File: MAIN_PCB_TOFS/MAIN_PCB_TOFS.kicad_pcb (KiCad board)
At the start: 2 copper layers, 60 x 84 mm, 13 parts, among them J1 Capteur Matricielle, J11 Capteur Matricielle, J12 SERVO m3, J13 SERVO m4, J2 Capteur Matricielle, J3 SERVO m2, J4 SERVO m1, J5 COMM_inter_mcu, U1 ESP32

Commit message: petites modifs kicad
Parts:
- added C1: 100n, Capacitor_SMD:C_0603_1608Metric, F.Cu at (126.2, 121.0)
- added C13: 100n, Capacitor_SMD:C_0603_1608Metric, F.Cu at (130.2, 121.0)
- added C2: 100u, Capacitor_SMD:CP_Elec_6.3x5.8, F.Cu at (109.1, 106.5)
- added C3: 100u, Capacitor_SMD:CP_Elec_6.3x5.8, F.Cu at (109.1, 114.6)
- added C4: 100u, Capacitor_SMD:CP_Elec_6.3x5.8, F.Cu at (109.1, 122.8)
- added C5: 10u, Capacitor_SMD:C_0603_1608Metric, F.Cu at (126.2, 123.5)
- added C6: 100n, Capacitor_SMD:C_0603_1608Metric, F.Cu at (126.2, 126.0)
- added C7: 100n, Capacitor_SMD:C_0603_1608Metric, F.Cu at (126.2, 128.5)
- added C8: 100n, Capacitor_SMD:C_0603_1608Metric, F.Cu at (126.2, 131.0)
- added D2: WS2812B, LED_SMD:LED_WS2812B_PLCC4_5.0x5.0mm_P3.2mm, F.Cu at (107.9, 130.2)
- added J1: TOF 2, Connector_PinHeader_2.54mm:PinHeader_1x06_P2.54mm_Vertical, F.Cu at (126.5, 104.7)
- added J2: TOF 3, Connector_PinHeader_2.54mm:PinHeader_1x06_P2.54mm_Vertical, F.Cu at (131.0, 104.7)
- added J6: TOF 1, Connector_PinHeader_2.54mm:PinHeader_1x06_P2.54mm_Vertical, F.Cu at (135.6, 104.7)
- added J7: Conn_01x02, Connector_PinHeader_2.54mm:PinHeader_1x02_P2.54mm_Vertical, F.Cu at (116.6, 125.4)
- added R1: 2.2k, Resistor_SMD:R_0603_1608Metric, F.Cu at (130.2, 123.5)
- added R2: 2.2k, Resistor_SMD:R_0603_1608Metric, F.Cu at (130.2, 126.0)
- added R3: 470R, Resistor_SMD:R_0603_1608Metric, F.Cu at (130.2, 128.5)
- added R4: 10k, Resistor_SMD:R_0603_1608Metric, F.Cu at (130.2, 131.0)
- added R5: 10k, Resistor_SMD:R_0603_1608Metric, F.Cu at (134.2, 121.0)
- added R6: 10k, Resistor_SMD:R_0603_1608Metric, F.Cu at (134.2, 123.5)
- added R7: 10k, Resistor_SMD:R_0603_1608Metric, F.Cu at (134.2, 126.0)
- added SW1: SW_SPDT, Button_Switch_SMD:SW_SPDT_PCM12, F.Cu at (119.2, 105.4)
- added SW2: SW_SPDT, Button_Switch_SMD:SW_SPDT_PCM12, F.Cu at (119.2, 112.3)
- added SW3: SW_SPDT, Button_Switch_SMD:SW_SPDT_PCM12, F.Cu at (119.2, 119.2)
- moved U1 12.6 mm to (97.6, 62.5)
- moved J1 8.94 mm to (133.0, 65.4)
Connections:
- U1 pad 11: unconnected-(U1-D35-Pad11) -> /Switch_terrain
- U1 pad 12: unconnected-(U1-D34-Pad12) -> /Switch_mode
- U1 pad 13: unconnected-(U1-UN-Pad13) -> /Tirette
- U1 pad 14: unconnected-(U1-UP-Pad14) -> /Switch_debug
- U1 pad 18: /SERVO_4 -> /SERVO_2
- U1 pad 19: /SERVO_3 -> unconnected-(U1-D2-Pad19)
- U1 pad 20: unconnected-(U1-D4-Pad20) -> /LPN2
- U1 pad 24: /SERVO_2 -> /LPN3
- U1 pad 30: unconnected-(U1-D23-Pad30) -> /LPN1
- U1 pad 5: /LED_IHM_2 -> /LED_IHM
- U1 pad 6: /LED_IHM_1 -> /SERVO_3
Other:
- board size 60 x 84 mm -> 88 x 84 mm

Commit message: organisation du pcb IHM pour préparer le routage
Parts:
- removed D4: GREEN_LED, LED_SMD:LED_0603_1608Metric
- removed D5: RED_LED, LED_SMD:LED_0603_1608Metric
- removed the J1 at (133.0, 65.4)
- removed J11: Capteur Matricielle, Connector_PinHeader_2.54mm:PinHeader_1x07_P2.54mm_Vertical
- removed J13: SERVO m4, Connector_PinHeader_2.54mm:PinHeader_1x03_P2.54mm_Vertical
- removed the J2 at (148.8, 65.1)
- removed R12, R13: 330R, Resistor_SMD:R_0603_1608Metric
- added H1: MountingHole_Pad, MountingHole:MountingHole_3.2mm_M3_Pad_Via, F.Cu at (83.5, 57.5)
- added H2: MountingHole_Pad, MountingHole:MountingHole_3.2mm_M3_Pad_Via, F.Cu at (139.4, 57.5)
- added H3: MountingHole_Pad, MountingHole:MountingHole_3.2mm_M3_Pad_Via, F.Cu at (139.4, 132.5)
- added H4: MountingHole_Pad, MountingHole:MountingHole_3.2mm_M3_Pad_Via, F.Cu at (83.5, 132.5)
- SW1: value SW_SPDT -> DEBUG
- SW2: value SW_SPDT -> TERRAIN
- SW3: value SW_SPDT -> MODE
- U1: footprint Library:PinHeader_2x15_P2.54mm_Vertical_esp32 -> Library:DIP-30_W25.4mm_LongPads_esp32
- moved J12 66.8 mm to (92.5, 57.7), turned to 90 degrees
- moved R7 66.0 mm to (86.0, 80.9), turned to 90 degrees
- moved J7 60.7 mm to (86.0, 73.0)
- moved C4 58.5 mm to (108.5, 64.3)
- moved C7 57.5 mm to (124.9, 71.0), turned to 180 degrees
- moved C3 52.3 mm to (95.0, 64.3)
- moved J3 47.2 mm to (105.7, 57.7), turned to 90 degrees
- moved R3 44.5 mm to (88.4, 113.1), turned to -90 degrees
- moved R1 44.1 mm to (125.7, 79.6), turned to -90 degrees
- moved C2 44.0 mm to (121.4, 64.3)
- moved C1 44.0 mm to (82.8, 113.7)
- moved C8 42.7 mm to (135.7, 89.4), turned to -90 degrees
- moved J4 40.9 mm to (118.3, 57.8), turned to 90 degrees
- moved R2 39.0 mm to (125.6, 87.2), turned to 90 degrees
- moved SW1 36.1 mm to (96.6, 133.5)
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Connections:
- J12 pad 1: /D18 -> /SERVO_3
- J3 pad 1: /D18 -> /SERVO_2
- J4 pad 1: /D19 -> /SERVO_1
- U1 pad 20: /LPN2 -> /LPN1
- U1 pad 30: /LPN1 -> /LPN2
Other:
- board size 88 x 84 mm -> 64.9 x 84 mm
- board text added: "Auto"
- board text added: "Bleu"
- board text added: "Jaune"
- board text added: "Manuel"
- board text added: "OFF"
- board text added: "ON"

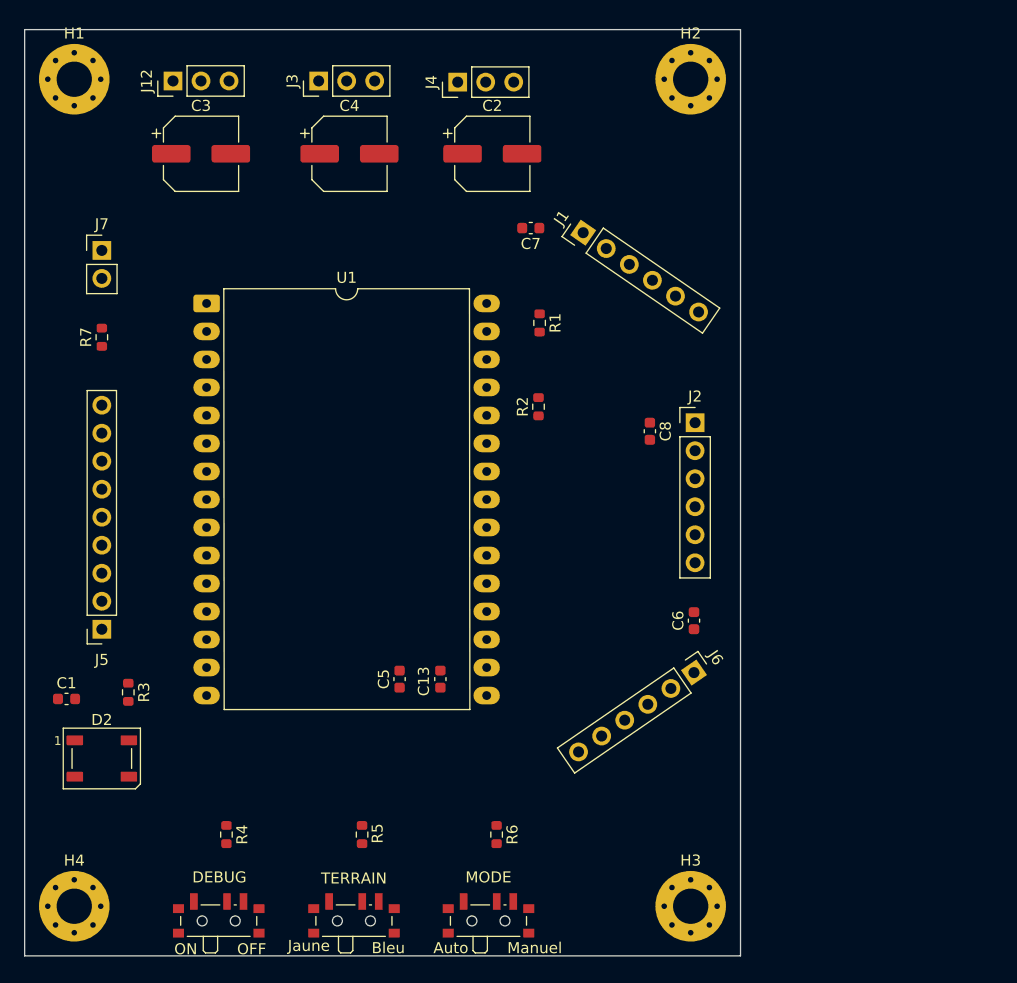
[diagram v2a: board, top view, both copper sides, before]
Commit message: modifications finales du pcb, problème sens capteurs tofs à régler
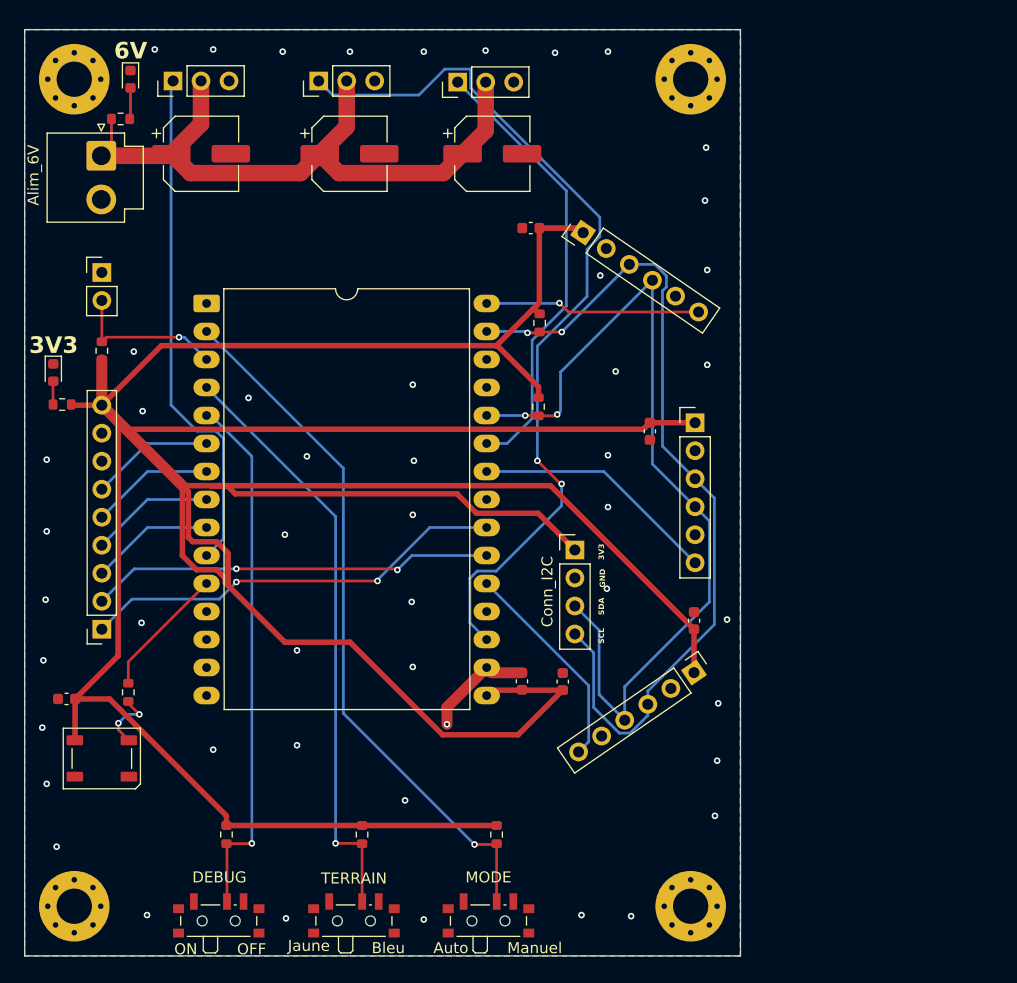
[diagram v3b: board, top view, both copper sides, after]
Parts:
- added D4: GREEN_LED, LED_SMD:LED_0603_1608Metric, F.Cu at (88.6, 57.5)
- added D5: GREEN_LED, LED_SMD:LED_0603_1608Metric, F.Cu at (81.6, 84.1)
- added J8: Alim_6V, Connector_JST:JST_VH_B2P-VH_1x02_P3.96mm_Vertical, F.Cu at (86.0, 64.4)
- added J9: Conn_I2C, Connector_PinHeader_2.54mm:PinHeader_1x04_P2.54mm_Vertical, F.Cu at (128.9, 100.2)
- added R12: 1k, Resistor_SMD:R_0603_1608Metric, F.Cu at (87.7, 61.1)
- added R13: 330R, Resistor_SMD:R_0603_1608Metric, F.Cu at (82.4, 87.0)
- moved C13 11.1 mm to (127.8, 112.1)
- moved C5 11.1 mm to (124.1, 112.1)
- moved J7 2.00 mm to (86.0, 75.0)
- moved R7 1.22 mm to (86.0, 82.1)
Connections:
- J5 pad 8: /6V -> unconnected-(J5-Pin_8-Pad8)
- U1 pad 11: /Switch_terrain -> /Switch_debug
- U1 pad 12: /Switch_mode -> /Switch_terrain
- U1 pad 14: /Switch_debug -> /Switch_mode
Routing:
- net /3V3: track 0.00 -> 369.6 mm
- net /SERVO_2: track 0.00 -> 80.3 mm, vias 0 -> 2
- net /SDA: track 0.00 -> 79.7 mm, vias 0 -> 2
- net /SCL: track 0.00 -> 77.7 mm, vias 0 -> 2
- net /Switch_mode: track 0.00 -> 63.9 mm, vias 0 -> 1
- net /6V: track 0.00 -> 62.2 mm
- net /Switch_terrain: track 0.00 -> 53.9 mm, vias 0 -> 1
- net /Switch_debug: track 0.00 -> 48.3 mm, vias 0 -> 1
- net /SERVO_3: track 0.00 -> 46.7 mm
- net /SERVO_1: track 0.00 -> 40.9 mm
- net /TX_ESP32: track 0.00 -> 38.8 mm, vias 0 -> 2
- net /RX_ESP32: track 0.00 -> 36.8 mm, vias 0 -> 2
- net /LPN3: track 0.00 -> 22.3 mm
- net /LPN2: track 0.00 -> 19.6 mm, vias 0 -> 1
- net /LPN1: track 0.00 -> 19.5 mm
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- added copper zone on B.Cu, net GND
- added copper zone on F.Cu, net GND
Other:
- board text added: "3V3"
- board text added: "6V"
- board text added: "GND"
- board text added: "SCL"
- board text added: "SDA"

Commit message: finalisation du pcb et création des fichiers nécéssaires
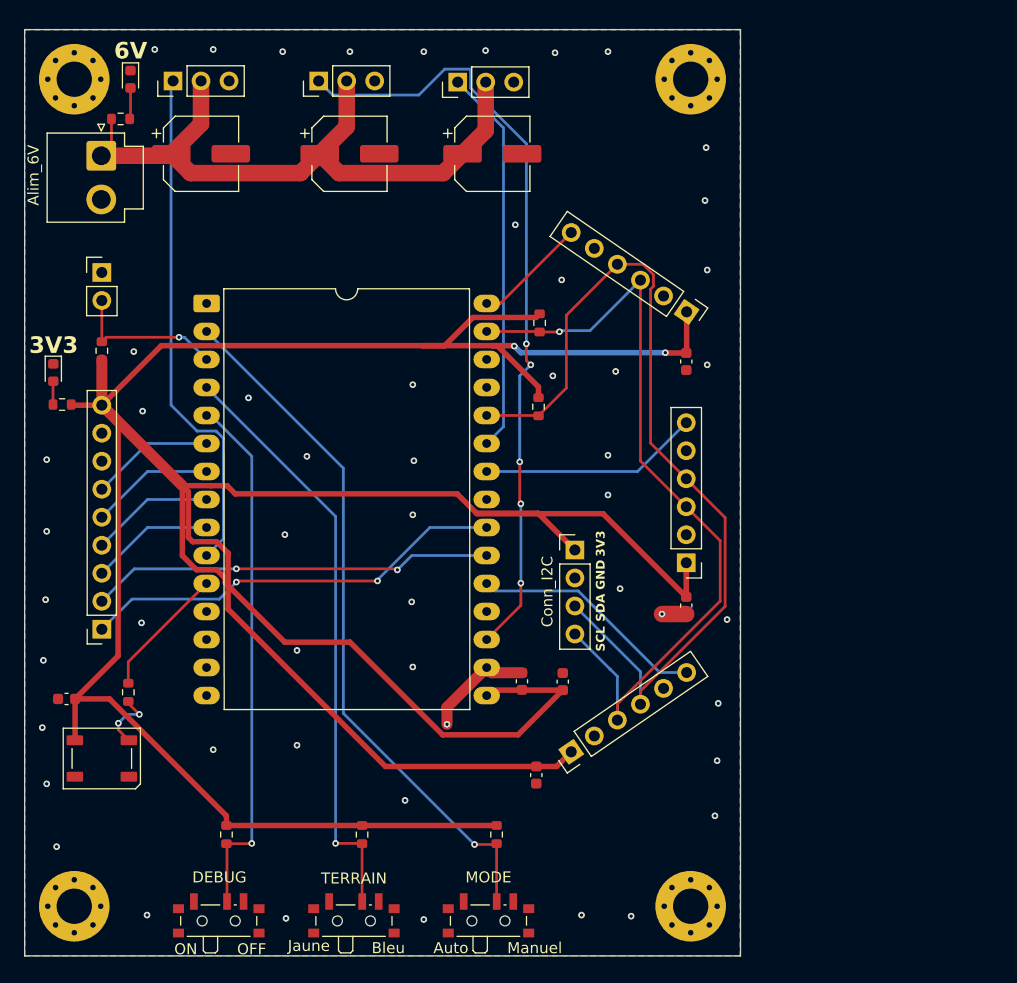
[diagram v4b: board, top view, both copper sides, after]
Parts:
- moved C6 20.0 mm to (125.4, 120.6), turned to -90 degrees
- moved C7 18.6 mm to (139.0, 83.1), turned to -90 degrees
- moved C8 16.1 mm to (139.0, 105.2)
- moved J6 13.3 mm to (128.6, 118.5), turned to 124.5 degrees
- moved J2 12.7 mm to (139.0, 101.3), turned to 180 degrees
- moved J1 11.8 mm to (139.0, 78.6), turned to -124.5 degrees
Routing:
- net /3V3: track 369.6 -> 340.7 mm, vias 0 -> 2
- net /SERVO_2: track 80.3 -> 71.0 mm, vias 2 -> 5
- net /LPN2: track 19.6 -> 10.3 mm, vias 1 -> 0
- net /SERVO_1: track 40.9 -> 35.1 mm
- net /SCL: track 77.7 -> 72.2 mm, vias 2 -> 1
- net /LPN3: track 22.3 -> 19.9 mm
- net GND: track 10.0 -> 12.2 mm, vias 49 -> 52
- net /LPN1: track 19.5 -> 21.5 mm
- net /SDA: track 79.7 -> 81.5 mm, vias 2 -> 0

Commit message: changement de la forme du pcb
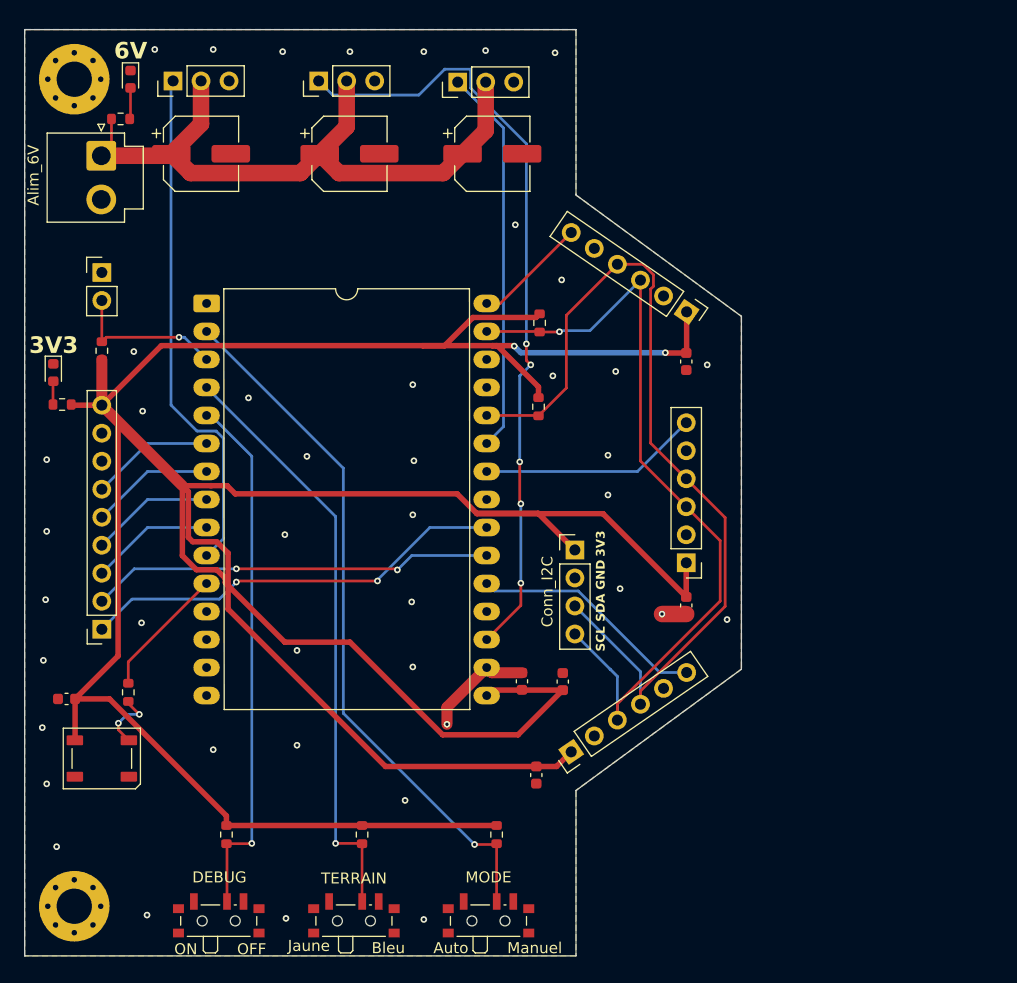
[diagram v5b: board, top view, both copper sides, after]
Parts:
- removed H2, H3: MountingHole_Pad, MountingHole:MountingHole_3.2mm_M3_Pad_Via
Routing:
- net GND: vias 52 -> 43
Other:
- board size 64.9 x 84 mm -> 65 x 84 mm
